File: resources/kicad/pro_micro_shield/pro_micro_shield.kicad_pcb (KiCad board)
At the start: 2 copper layers, 34.5 x 45.8 mm, 14 parts, among them U0 ProMicro

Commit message: cleanup resources and shield gerber files
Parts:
- moved H2 36.2 mm to (188.5, 74.0)
- moved JS0 2.25 mm to (189.0, 86.4)
- moved JS1 2.25 mm to (189.0, 97.0)
- moved JS2 2.25 mm to (189.0, 107.5)
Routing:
- net Net-(JS1-Pad3): track 37.5 -> 35.3 mm
- net Net-(JS0-Pad3): track 48.4 -> 46.1 mm
- net Net-(JS2-Pad3): track 27.0 -> 26.3 mm
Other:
- board text added: "start button resistor (1K)"
- board text removed: "10K"
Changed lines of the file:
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@@
     (thickness 1.6)
     (drawings 51)
-    (tracks 31)
+    (tracks 30)
     (zones 0)
     (modules 14)
@@
     (solder_mask_min_width 0.25)
     (aux_axis_origin 0 0)
-    (visible_elements FFFFFF7F)
+    (visible_elements FFFFEF7F)
     (pcbplotparams
       (layerselection 0x010fc_ffffffff)
@@
   )
   (module MountingHole:MountingHole_2.2mm_M2 (layer F.Cu)
-    (at 188.5 110.25)
+    (at 188.5 74)
     (descr "Mounting Hole 2.2mm, no annular, M2")
     (tags "mounting hole 2.2mm no annular m2")
@@
   )
   (module Connector_Wire:SolderWirePad_1x03_P3.175mm_Drill1mm (layer F.Cu)
-    (at 189 105.25 90)
+    (at 189 107.5 90)
     (descr "Wire solder connection")
     (tags connector)
@@
   )
   (module Connector_Wire:SolderWirePad_1x03_P3.175mm_Drill1mm (layer F.Cu)
-    (at 189 94.75 90)
+    (at 189 97 90)
     (descr "Wire solder connection")
     (tags connector)
@@
   )
   (module Connector_Wire:SolderWirePad_1x03_P3.175mm_Drill1mm (layer F.Cu)
-    (at 189 84.175 90)
+    (at 189 86.425 90)
     (descr "Wire solder connection")
     (tags connector)
@@
       (net 1 GND))
   )
-  (gr_text 10K (at 160.25 110.5 270) (layer F.SilkS)
-    (effects (font (size 1 1) (thickness 0.15)))
+  (gr_text "start button\nresistor\n(1K)" (at 161 110.75 270) (layer F.SilkS)
+    (effects (font (size 0.8 0.8) (thickness 0.15)))
   )
   (gr_text "START BUTTON" (at 163.5 93.5 270) (layer F.SilkS)
@@
     (effects (font (size 2 2) (thickness 0.3)))
   )
-  (gr_text "SENSOR 3" (at 185.5 102.25 90) (layer F.SilkS)
-    (effects (font (size 1 1) (thickness 0.15)))
-  )
-  (gr_text "SENSOR 2" (at 185.5 91.75 90) (layer F.SilkS)
-    (effects (font (size 1 1) (thickness 0.15)))
-  )
-  (gr_text "SENSOR 1" (at 185.5 81.25 90) (layer F.SilkS)
+  (gr_text "SENSOR 3" (at 185.5 104.5 90) (layer F.SilkS)
+    (effects (font (size 1 1) (thickness 0.15)))
+  )
+  (gr_text "SENSOR 2" (at 185.5 94 90) (layer F.SilkS)
+    (effects (font (size 1 1) (thickness 0.15)))
+  )
+  (gr_text "SENSOR 1" (at 185.5 83.5 90) (layer F.SilkS)
     (effects (font (size 1 1) (thickness 0.15)))
   )
@@
     (effects (font (size 1 1) (thickness 0.15)))
   )
-  (gr_text D8 (at 187 99 90) (layer F.SilkS)
-    (effects (font (size 1 1) (thickness 0.15)))
-  )
-  (gr_text D7 (at 187 88.25 90) (layer F.SilkS)
-    (effects (font (size 1 1) (thickness 0.15)))
-  )
-  (gr_text D6 (at 187 77.75 90) (layer F.SilkS)
-    (effects (font (size 1 1) (thickness 0.15)))
-  )
-  (gr_text D4 (at 180.25 111.5) (layer F.SilkS)
+  (gr_text D8 (at 187 101.25 90) (layer F.SilkS)
+    (effects (font (size 1 1) (thickness 0.15)))
+  )
+  (gr_text D7 (at 187 90.5 90) (layer F.SilkS)
+    (effects (font (size 1 1) (thickness 0.15)))
+  )
+  (gr_text D6 (at 187 80 90) (layer F.SilkS)
+    (effects (font (size 1 1) (thickness 0.15)))
+  )
+  (gr_text D3 (at 180.25 111.5) (layer F.SilkS)
     (effects (font (size 1 1) (thickness 0.15)))
   )
@@
     (effects (font (size 1 1) (thickness 0.15)))
   )
-  (gr_text VCC (at 187 84.25 90) (layer F.SilkS)
-    (effects (font (size 1 1) (thickness 0.15)))
-  )
-  (gr_text VCC (at 187 94.75 90) (layer F.SilkS)
-    (effects (font (size 1 1) (thickness 0.15)))
-  )
-  (gr_text VCC (at 187 105.25 90) (layer F.SilkS)
+  (gr_text VCC (at 187 86.5 90) (layer F.SilkS)
+    (effects (font (size 1 1) (thickness 0.15)))
+  )
+  (gr_text VCC (at 187 97 90) (layer F.SilkS)
+    (effects (font (size 1 1) (thickness 0.15)))
+  )
+  (gr_text VCC (at 187 107.5 90) (layer F.SilkS)
     (effects (font (size 1 1) (thickness 0.15)))
   )
@@
     (effects (font (size 1 1) (thickness 0.15)))
   )
-  (gr_text GND (at 187 81 90) (layer F.SilkS)
-    (effects (font (size 1 1) (thickness 0.15)))
-  )
-  (gr_text GND (at 187 91.5 90) (layer F.SilkS)
-    (effects (font (size 1 1) (thickness 0.15)))
-  )
-  (gr_text GND (at 187 102 90) (layer F.SilkS)
+  (gr_text GND (at 187 83.25 90) (layer F.SilkS)
+    (effects (font (size 1 1) (thickness 0.15)))
+  )
+  (gr_text GND (at 187 93.75 90) (layer F.SilkS)
+    (effects (font (size 1 1) (thickness 0.15)))
+  )
+  (gr_text GND (at 187 104.25 90) (layer F.SilkS)
     (effects (font (size 1 1) (thickness 0.15)))
   )
@@
     (effects (font (size 1 1) (thickness 0.15)))
   )
-  (segment (start 177.03 103.5) (end 167.756299 94.226299) (width 0.25) (layer F.Cu) (net 3))
-  (segment (start 189 77.825) (end 184.5 82.325) (width 0.25) (layer F.Cu) (net 3))
-  (segment (start 182.80218 103.5) (end 177.03 103.5) (width 0.25) (layer F.Cu) (net 3))
-  (segment (start 184.5 82.325) (end 184.5 101.80218) (width 0.25) (layer F.Cu) (net 3))
-  (segment (start 184.5 101.80218) (end 182.80218 103.5) (width 0.25) (layer F.Cu) (net 3))
-  (segment (start 167.756299 94.226299) (end 166.88 93.35) (width 0.25) (layer F.Cu) (net 3))
+  (segment (start 184.5 84.575) (end 189 80.075) (width 0.25) (layer F.Cu) (net 3))
+  (segment (start 184.5 101.80218) (end 184.5 84.575) (width 0.25) (layer F.Cu) (net 3))
+  (segment (start 182.80218 103.5) (end 184.5 101.80218) (width 0.25) (layer F.Cu) (net 3))
+  (segment (start 177.03 103.5) (end 182.80218 103.5) (width 0.25) (layer F.Cu) (net 3))
+  (segment (start 166.88 93.35) (end 177.03 103.5) (width 0.25) (layer F.Cu) (net 3))
   (segment (start 166.88 95.89) (end 174.99 104) (width 0.25) (layer F.Cu) (net 4))
-  (segment (start 185 101.93859) (end 185 92.4) (width 0.25) (layer F.Cu) (net 4))
   (segment (start 182.93859 104) (end 185 101.93859) (width 0.25) (layer F.Cu) (net 4))
-  (segment (start 187.750321 89.649679) (end 189 88.4) (width 0.25) (layer F.Cu) (net 4))
   (segment (start 174.99 104) (end 182.93859 104) (width 0.25) (layer F.Cu) (net 4))
-  (segment (start 185 92.4) (end 187.750321 89.649679) (width 0.25) (layer F.Cu) (net 4))
-  (segment (start 188.675 98.9) (end 189 98.9) (width 0.25) (layer F.Cu) (net 5))
+  (segment (start 185 94.65) (end 189 90.65) (width 0.25) (layer F.Cu) (net 4))
+  (segment (start 185 101.93859) (end 185 94.65) (width 0.25) (layer F.Cu) (net 4))
+  (segment (start 188.675 101.15) (end 189 101.15) (width 0.25) (layer F.Cu) (net 5))
   (segment (start 172.95 104.5) (end 183.075 104.5) (width 0.25) (layer F.Cu) (net 5))
-  (segment (start 183.075 104.5) (end 188.675 98.9) (width 0.25) (layer F.Cu) (net 5))
   (segment (start 166.88 98.43) (end 172.95 104.5) (width 0.25) (layer F.Cu) (net 5))
+  (segment (start 186.425 101.15) (end 189 101.15) (width 0.25) (layer F.Cu) (net 5))
+  (segment (start 183.075 104.5) (end 186.425 101.15) (width 0.25) (layer F.Cu) (net 5))
   (segment (start 171.06 87.37) (end 166.88 83.19) (width 0.25) (layer B.Cu) (net 17))
   (segment (start 171.06 107.25) (end 171.06 87.37) (width 0.25) (layer B.Cu) (net 17))

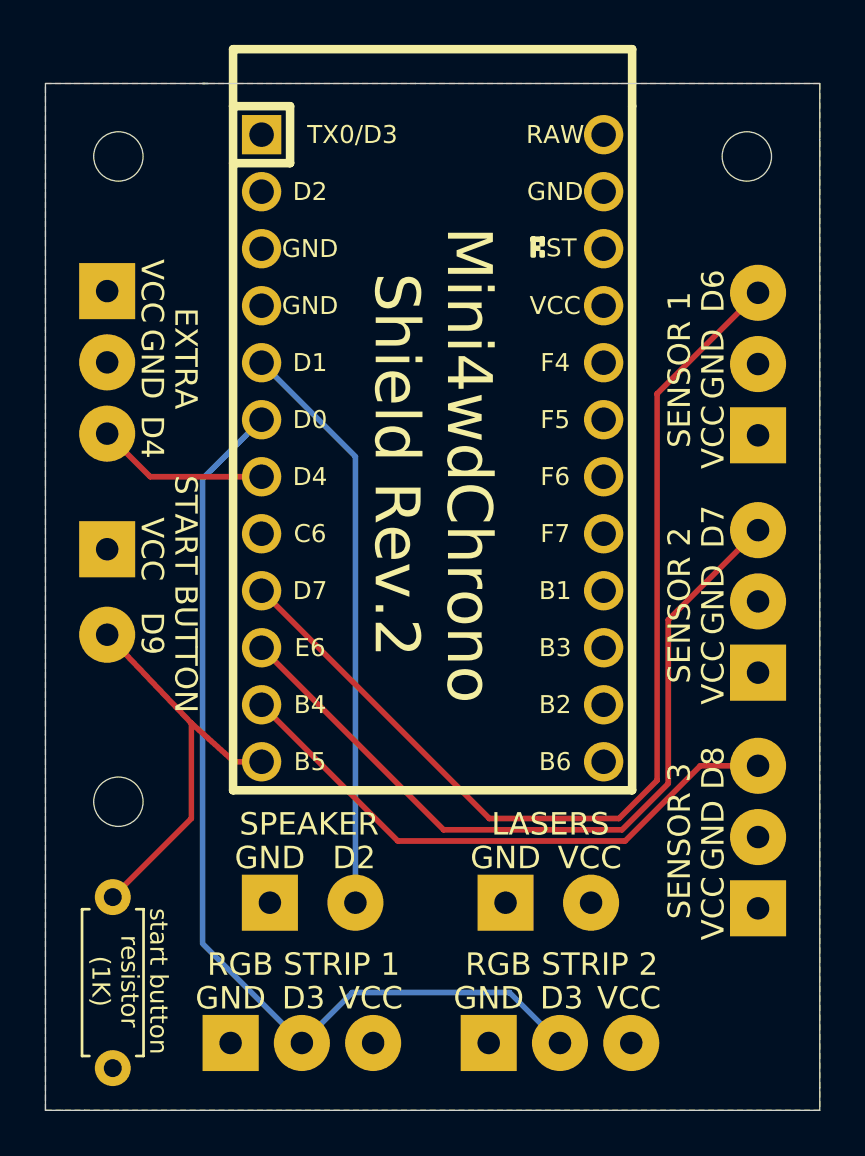
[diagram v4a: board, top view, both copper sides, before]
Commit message: use standard 2.54mm header pins in arduino shield
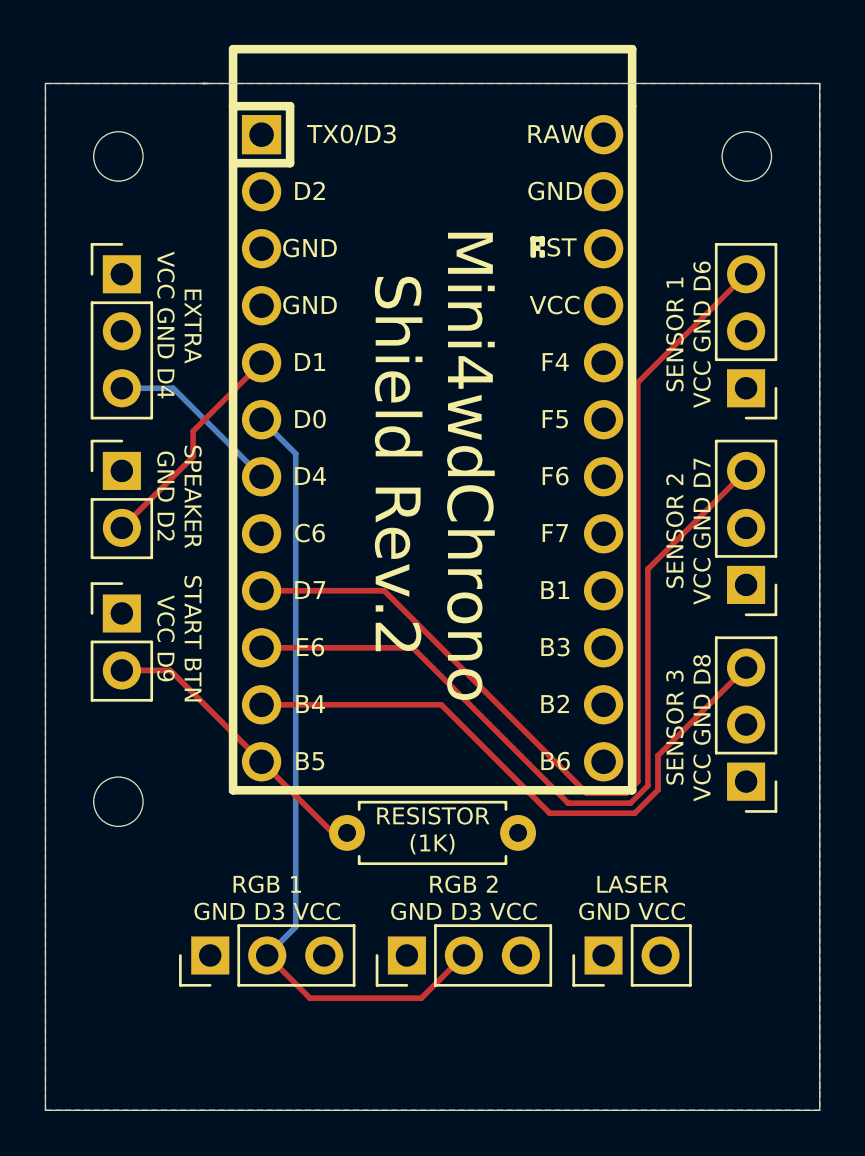
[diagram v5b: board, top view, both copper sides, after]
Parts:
- JBUTTON0, JLASER0, JSPEAKER0: footprint Connector_Wire:SolderWirePad_1x02_P3.81mm_Drill1mm -> Connector_PinHeader_2.54mm:PinHeader_1x02_P2.54mm_Vertical
- JEX0, JRGB0, JRGB1, JS0, JS1, JS2: footprint Connector_Wire:SolderWirePad_1x03_P3.175mm_Drill1mm -> Connector_PinHeader_2.54mm:PinHeader_1x03_P2.54mm_Vertical
- moved JSPEAKER0 20.3 mm to (160.7, 88.0)
- moved R0 10.8 mm to (170.7, 104.1), turned to 0 degrees
- moved JS2 5.67 mm to (188.5, 101.9), turned to 180 degrees
- moved JRGB1 5.34 mm to (173.4, 109.6), turned to 90 degrees
- moved JLASER0 4.96 mm to (182.1, 109.6), turned to 90 degrees
- moved JRGB0 4.00 mm to (164.6, 109.6), turned to 90 degrees
- moved JS1 3.95 mm to (188.5, 93.1), turned to 180 degrees
- moved JBUTTON0 2.94 mm to (160.7, 94.4), turned to 0 degrees
- moved JS0 2.16 mm to (188.5, 84.3), turned to 180 degrees
- moved JEX0 1.00 mm to (160.7, 79.2), turned to 0 degrees
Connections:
- U0 pad 1: Net-(U0-Pad1) -> (no net)
- U0 pad 13: Net-(U0-Pad13) -> (no net)
- U0 pad 14: Net-(U0-Pad14) -> (no net)
- U0 pad 15: Net-(U0-Pad15) -> (no net)
- U0 pad 16: Net-(U0-Pad16) -> (no net)
- U0 pad 17: Net-(U0-Pad17) -> (no net)
- U0 pad 18: Net-(U0-Pad18) -> (no net)
- U0 pad 19: Net-(U0-Pad19) -> (no net)
- U0 pad 2: Net-(U0-Pad2) -> (no net)
- U0 pad 20: Net-(U0-Pad20) -> (no net)
- U0 pad 22: Net-(U0-Pad22) -> (no net)
- U0 pad 24: Net-(U0-Pad24) -> (no net)
- U0 pad 8: Net-(U0-Pad8) -> (no net)
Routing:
- net Net-(JSPEAKER0-Pad2): track 25.8 -> 9.94 mm
- net Net-(JRGB0-Pad2): track 44.0 -> 35.4 mm
- net Net-(JBUTTON0-Pad2): track 18.4 -> 13.0 mm
- net Net-(JS1-Pad3): track 35.3 -> 36.2 mm
- net Net-(JS2-Pad3): track 26.3 -> 27.2 mm
- net Net-(JS0-Pad3): track 46.1 -> 45.3 mm
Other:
- board text added: "EXTRA VCC GND D4"
- board text added: "LASER GND VCC"
- board text added: "RESISTOR (1K)"
- board text added: "RGB 1 GND D3 VCC"
- board text added: "RGB 2 GND D3 VCC"
- board text added: "SENSOR 1 VCC GND D6"
- board text added: "SENSOR 2 VCC GND D7"
- board text added: "SENSOR 3 VCC GND D8"
- board text added: "SPEAKER GND D2"
- board text added: "START BTN VCC D9"
- board text removed: "D2"
- board text removed: "D3"
- board text removed: "D4"
- board text removed: "D6"
- board text removed: "D7"
- board text removed: "D8"
- board text removed: "D9"
- board text removed: "EXTRA"
- board text removed: "GND"
- board text removed: "LASERS"
- board text removed: "RGB STRIP 1"
- board text removed: "RGB STRIP 2"
- board text removed: "SENSOR 1"
- board text removed: "SENSOR 2"
- board text removed: "SENSOR 3"
- board text removed: "SPEAKER"
- board text removed: "START BUTTON"
- board text removed: "VCC"
- board text removed: "start button resistor (1K)"

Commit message: update shield gerber files
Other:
- rule pad_to_mask_clearance: 0.051 -> 0

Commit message: shield revision 3
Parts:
- removed JBUTTON0, JLASER0, JSPEAKER0: Conn_01x02_Female, Connector_PinHeader_2.54mm:PinHeader_1x02_P2.54mm_Vertical
- removed JEX0, JRGB0, JRGB1, JS0, JS1, JS2: Conn_01x03_Female, Connector_PinHeader_2.54mm:PinHeader_1x03_P2.54mm_Vertical
- removed R0: R_US, Resistor_THT:R_Axial_DIN0207_L6.3mm_D2.5mm_P7.62mm_Horizontal
- added J1: Conn_01x06_Female, Connector_PinHeader_2.54mm:PinHeader_1x06_P2.54mm_Vertical, F.Cu at (160.5, 94.3)
- added J2: Conn_01x06_Female, Connector_PinHeader_2.54mm:PinHeader_1x06_P2.54mm_Vertical, F.Cu at (181.1, 107.4)
- added J3: Conn_01x06_Female, Connector_PinHeader_2.54mm:PinHeader_1x06_P2.54mm_Vertical, F.Cu at (181.0, 112.5)
- added J4: Conn_01x09_Female, Connector_PinHeader_2.54mm:PinHeader_1x09_P2.54mm_Vertical, F.Cu at (188.5, 100.2)
- added R1: R, Resistor_THT:R_Axial_DIN0207_L6.3mm_D2.5mm_P15.24mm_Horizontal, F.Cu at (166.9, 104.2)
- renumbered H0 to H1, H1 to H2, H2 to H3, U0 to U1
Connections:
- U1 pad 1: (no net) -> unconnected-(U1-Pad1)
- U1 pad 10: Net-(JS1-Pad3) -> SIG1
- U1 pad 11: Net-(JS2-Pad3) -> SIG2
- U1 pad 12: Net-(JBUTTON0-Pad2) -> BTN0
- U1 pad 13: (no net) -> unconnected-(U1-Pad13)
- U1 pad 14: (no net) -> unconnected-(U1-Pad14)
- U1 pad 15: (no net) -> unconnected-(U1-Pad15)
- U1 pad 16: (no net) -> unconnected-(U1-Pad16)
- U1 pad 17: (no net) -> unconnected-(U1-Pad17)
- U1 pad 18: (no net) -> unconnected-(U1-Pad18)
- U1 pad 19: (no net) -> unconnected-(U1-Pad19)
- U1 pad 2: (no net) -> unconnected-(U1-Pad2)
- U1 pad 20: (no net) -> unconnected-(U1-Pad20)
- U1 pad 22: (no net) -> unconnected-(U1-Pad22)
- U1 pad 24: (no net) -> unconnected-(U1-Pad24)
- U1 pad 5: Net-(JSPEAKER0-Pad2) -> SPEAKER0
- U1 pad 6: Net-(JRGB0-Pad2) -> STRIP0
- U1 pad 7: Net-(JEX0-Pad3) -> D4
- U1 pad 8: (no net) -> C6
- U1 pad 9: Net-(JS0-Pad3) -> SIG0
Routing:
- net Net-(JS0-Pad3): track 45.3 -> 0.00 mm
- net SIG0: track 0.00 -> 44.8 mm
- net SIG1: track 0.00 -> 36.8 mm
- net Net-(JS1-Pad3): track 36.2 -> 0.00 mm
- net Net-(JRGB0-Pad2): track 35.4 -> 0.00 mm
- net STRIP0: track 0.00 -> 32.5 mm
- net C6: track 0.00 -> 31.6 mm
- net SIG2: track 0.00 -> 28.9 mm
- net D4: track 0.00 -> 27.2 mm
- net Net-(JS2-Pad3): track 27.2 -> 0.00 mm
- net BTN0: track 0.00 -> 15.1 mm
- net Net-(JBUTTON0-Pad2): track 13.0 -> 0.00 mm
- net Net-(JSPEAKER0-Pad2): track 9.94 -> 0.00 mm
- net Net-(JEX0-Pad3): track 7.86 -> 0.00 mm
- net SPEAKER0: track 0.00 -> 7.84 mm
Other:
- outline, holes or cut-outs redrawn
- net class Default removed
- board text added: "D4 VCC GND EXTRA"
- board text added: "D5 VCC GND EXTRA"
- board text added: "GND D3 VCC RGB STRIP"
- board text added: "GND VCC D4 EXTRA"
- board text added: "GND VCC D5 EXTRA"
- board text added: "LASER VCC GND"
- board text added: "Mini4wdChrono Shield Rev.3"
- board text added: "RESISTOR 1K"
- board text added: "SENSOR 1 D6 GND VCC"
- board text added: "SENSOR 2 D7 GND VCC"
- board text added: "SENSOR 3 D8 GND VCC"
- board text added: "SPEAKER D2 GND"
- board text added: "START BTN D9 VCC"
- board text added: "VCC D3 GND RGB STRIP"
- board text removed: "EXTRA VCC GND D4"
- board text removed: "Mini4wdChrono Shield Rev.2"
- board text removed: "RESISTOR (1K)"
- board text removed: "RGB 1 GND D3 VCC"
- board text removed: "RGB 2 GND D3 VCC"

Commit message: shield revision 3
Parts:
- removed the J3 at (181.0, 112.5)
- J2: value Conn_01x06_Female -> Conn_01x12_Female; footprint Connector_PinHeader_2.54mm:PinHeader_1x06_P2.54mm_Vertical -> Connector_PinHeader_2.54mm:PinHeader_1x12_P2.54mm_Vertical
- moved J2 20.7 mm to (160.5, 110.1), turned to 90 degrees
- moved J1 2.30 mm to (162.6, 93.3)
- moved J3 2.21 mm to (186.4, 101.0)
- moved R1 0.91 mm to (166.9, 105.2)
- renumbered J4 to J3
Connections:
- J2 pad 1: VCC -> D4
- J2 pad 2: STRIP0 -> VCC
- J2 pad 4: VCC -> C6
- J2 pad 5: STRIP0 -> VCC
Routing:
- net C6: track 31.6 -> 20.7 mm
- net STRIP0: track 32.5 -> 38.1 mm
- net D4: track 27.2 -> 24.6 mm
- net SPEAKER0: track 7.84 -> 5.36 mm
- net SIG2: track 28.9 -> 27.1 mm
- net SIG1: track 36.8 -> 35.0 mm
- net SIG0: track 44.8 -> 42.9 mm
- net BTN0: track 15.1 -> 16.2 mm
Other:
- board text added: "RESISTOR 1-10K"
- board text removed: "RESISTOR 1K"
